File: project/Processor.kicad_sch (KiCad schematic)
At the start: 22 parts, among them IC1 74HC138, IC2 W65C02, IC3 74HC00, IC4 SYSTEM ROM, IC5 W65C22, IC6 RAM, IC7 W65C22, IC8 W65C51, SW4 CLOCK INPUT, X5 EXT. CLOCK

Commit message: Fix grid issues, fix missing libraries, replace FT232 with FT231
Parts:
- C501: renamed from C1; value 100nF -> 100n
- C502: renamed from C2; value 100nF -> 100n
- C503: renamed from C3; value 100nF -> 100n
- C504: renamed from C4; value 100nF -> 100n
- C505: renamed from C5; value 100nF -> 100n
- C506: renamed from C6; value 100nF -> 100n
- C507: renamed from C7; value 100nF -> 100n
- C508: renamed from C8; value 30pF -> 30p
- X501: renamed from X5; footprint Connector_Coaxial:MMCX_Molex_73415-1471_Vertical -> Connector_Coaxial:SMA_Amphenol_901-144_Vertical; Mfr. Molex -> Amphenol RF; Mfr. No. 73415-1475 -> 901-144; Mouser 538-73415-1475 -> 523-901-144
- renumbered IC1 to IC501, IC2 to IC502, IC3 to IC503, IC4 to IC504, IC5 to IC505, IC6 to IC506, IC7 to IC507, IC8 to IC508, R4 to R501, R5 to R502, SW4 to SW501, XTAL1 to XTAL501, XTAL2 to XTAL502
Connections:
- no-connect marks 16 -> 15
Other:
- moved on the sheet: C508, R502, XTAL502

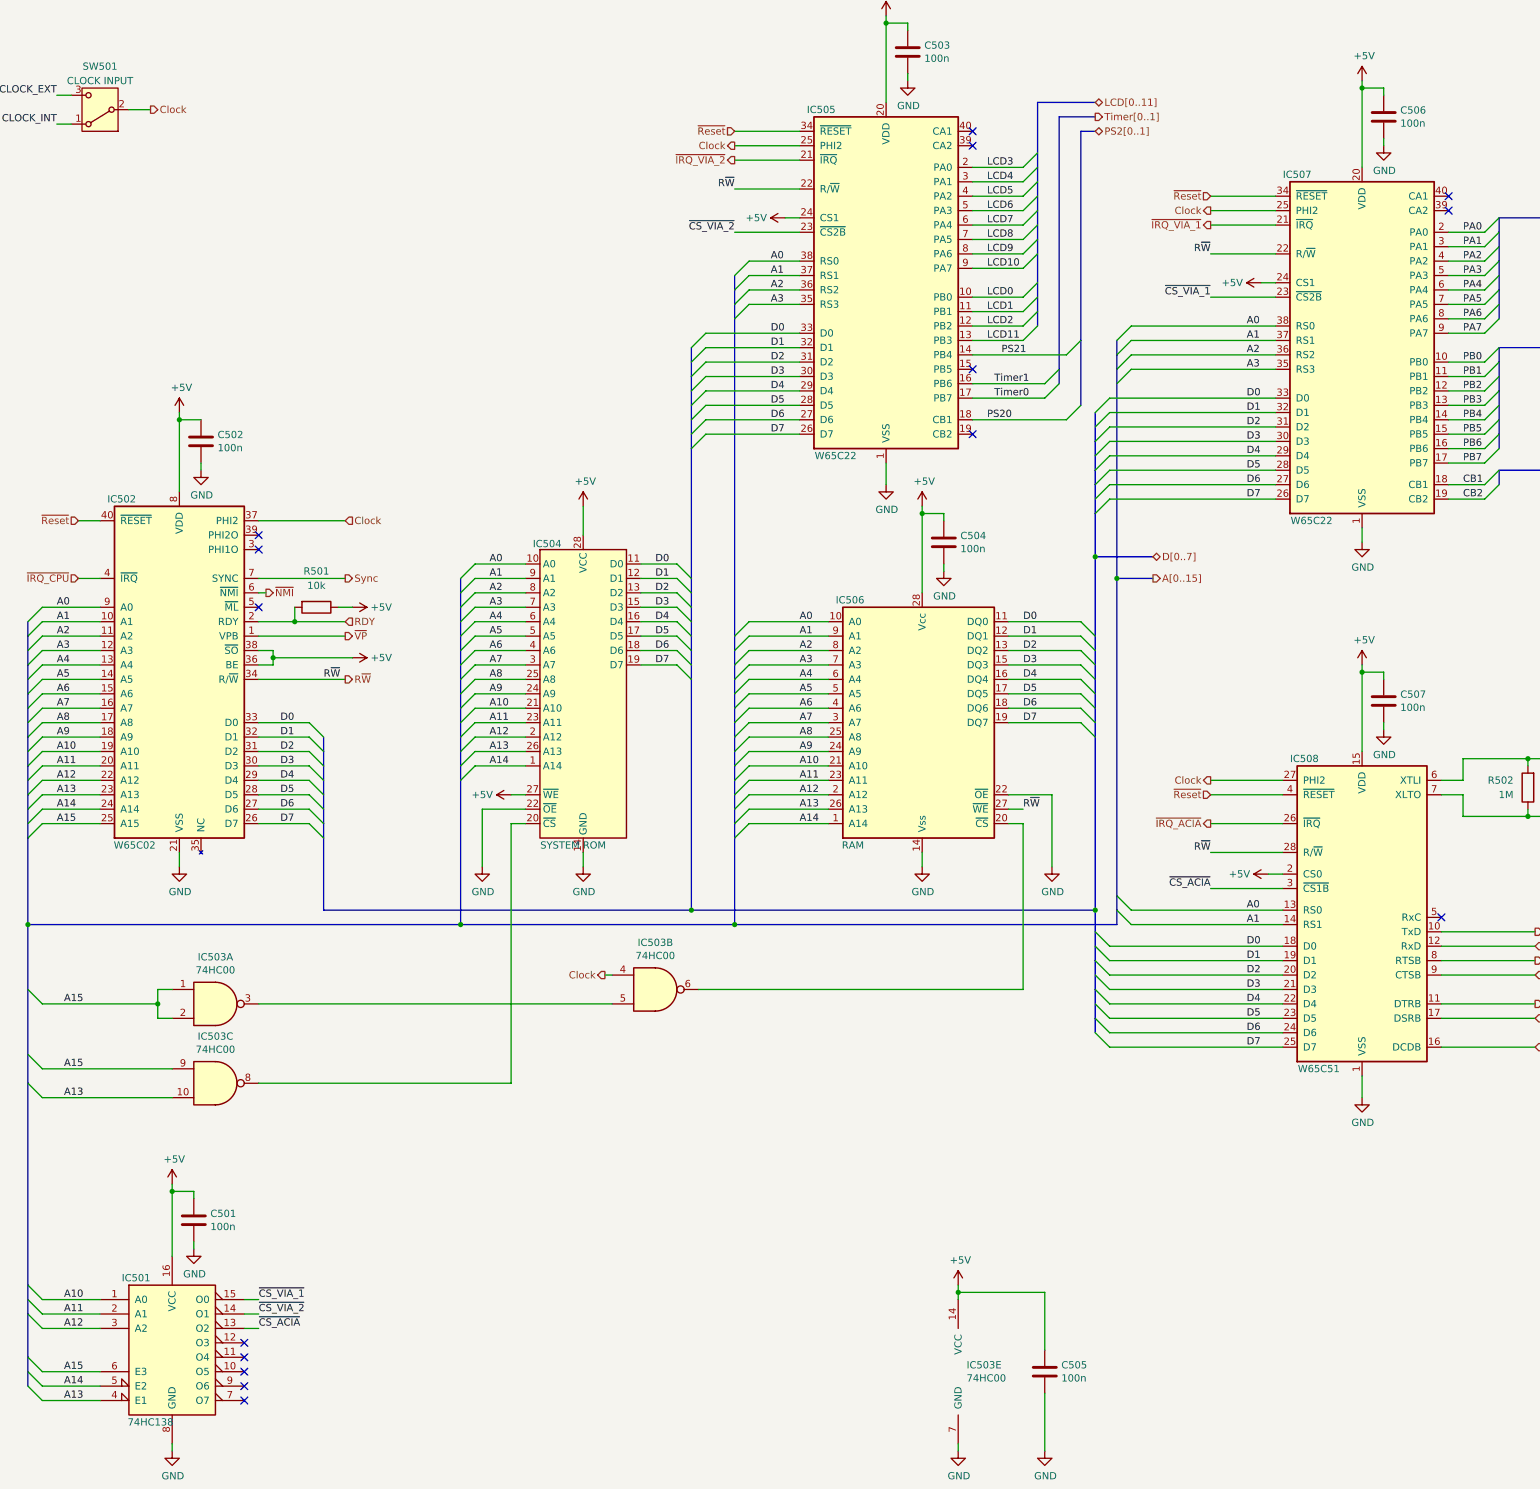
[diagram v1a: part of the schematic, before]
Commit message: Fix swapped DM and DP, add missing datasheets, remove Mouser property
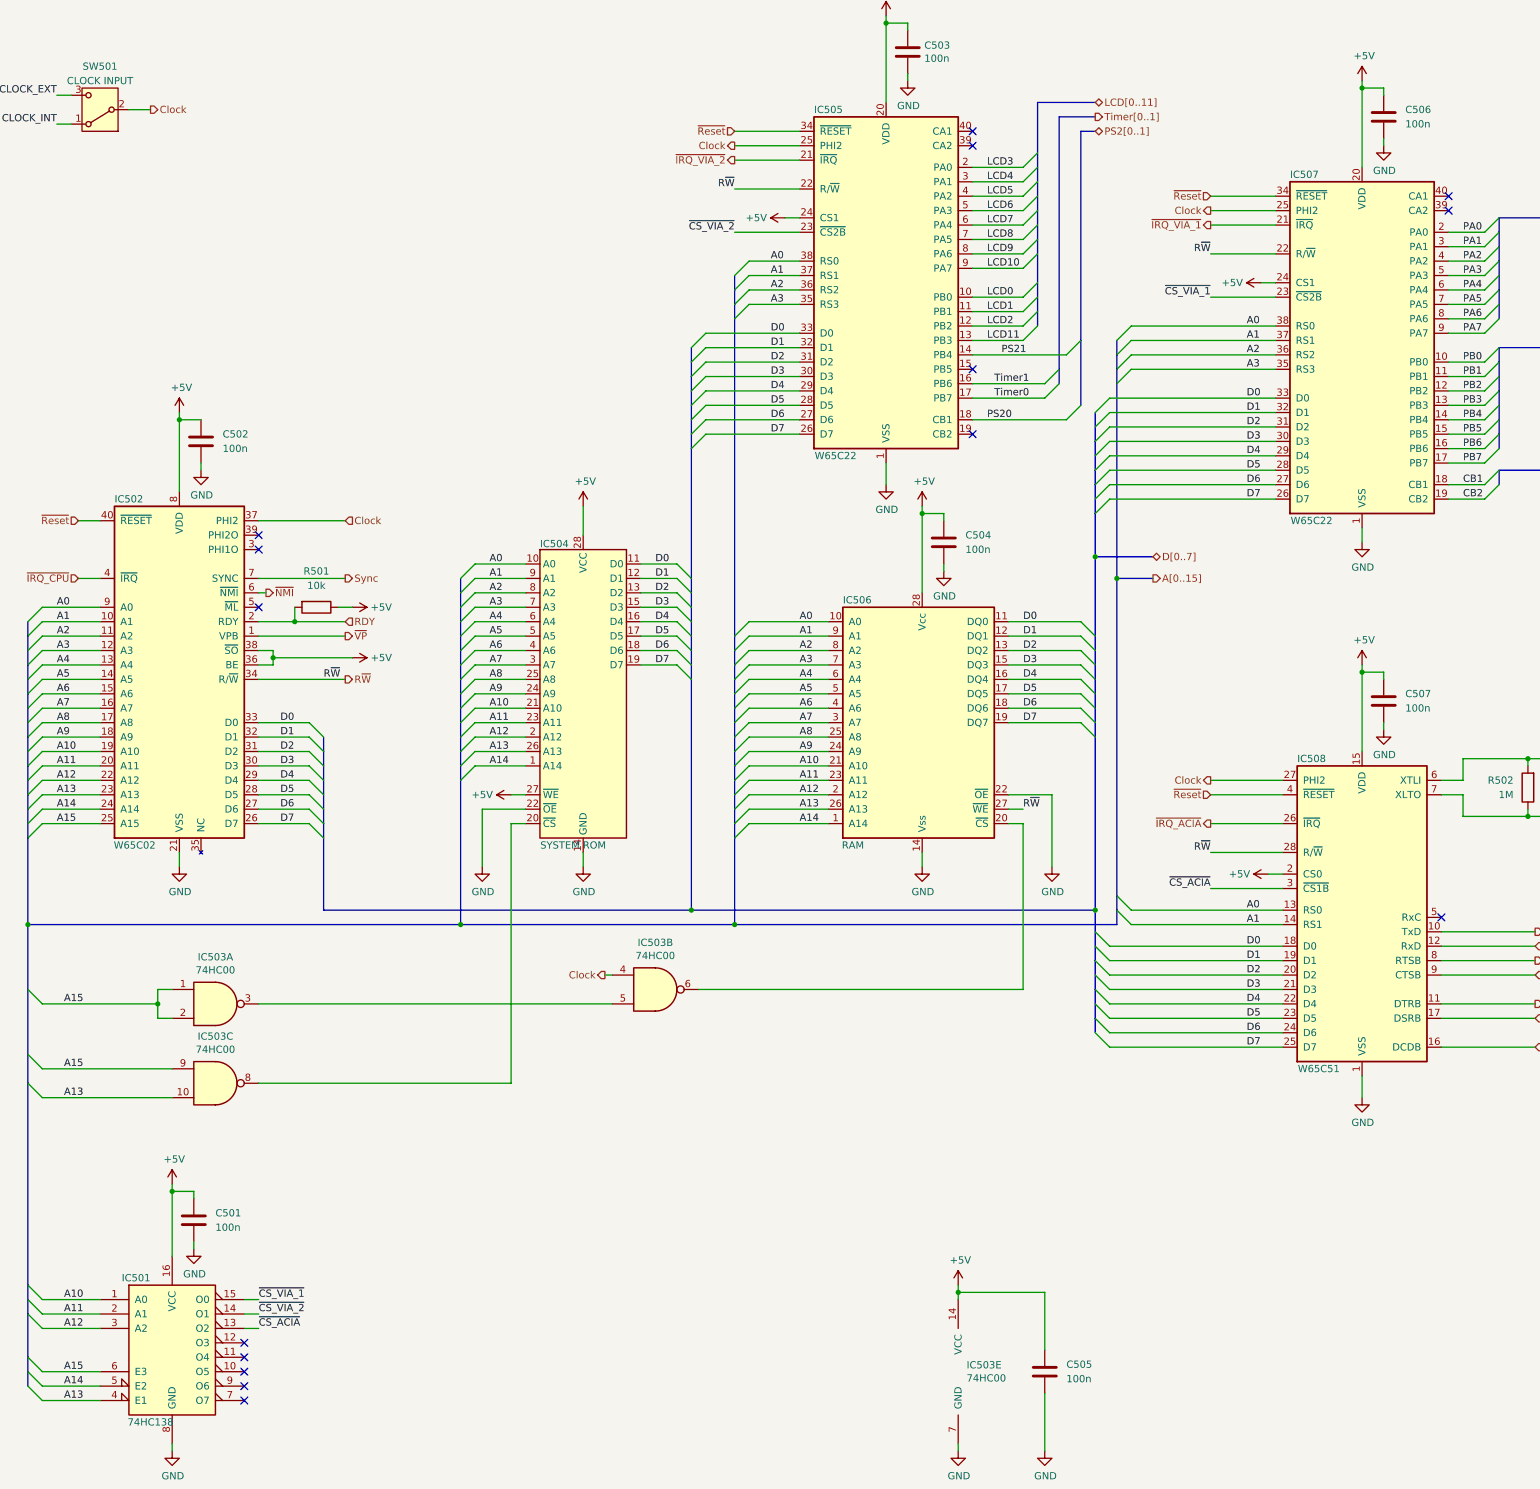
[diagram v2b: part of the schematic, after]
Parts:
- C501, C502, C503, C504, C505, C506, C507: Mouser 810-FA18X8R1H104KRU6 -> (none)
- C508: Mouser 80-C315C300JCG5TA -> (none)
- IC501: Mouser 595-SN74HC138AN -> (none)
- IC502: Mouser 955-W65C02S6TPG-14 -> (none)
- IC503: Mouser 595-SN74HC00AN -> (none)
- IC504: Mouser 556-AT28C25615PU -> (none)
- IC505: Mouser 955-W65C22S6TPG-14 -> (none)
- IC506: Mouser 913-AS6C62256-55PCN -> (none)
- IC508: Mouser 955-W65C51N6TPG-14 -> (none)
- R501: Mouser 603-MFP-25BRD52-10K -> (none)
- R502: Mouser 603-MFR-25FRE52-1M -> (none)
- SW501: Mouser 612-EG1271 -> (none)
- X501: Mouser 523-901-144 -> (none)
- XTAL501: Mouser 520-TCF100-X -> (none)
- XTAL502: Mouser 774-MP018B -> (none)
